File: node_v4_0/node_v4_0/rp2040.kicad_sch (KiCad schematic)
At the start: 29 parts, among them U1 RP2040, U2 W25Q128JVS, U7 PTS526 SK15 SMTR2 LFS, U8 PTS526 SK15 SMTR2 LFS

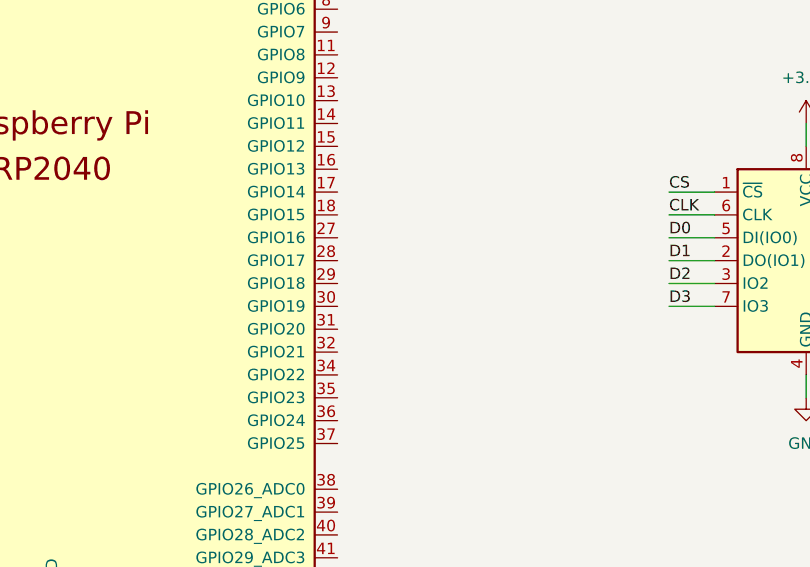
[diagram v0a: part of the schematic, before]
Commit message: more tracing, added RFM, added SIM, built power systems. converted to star ground
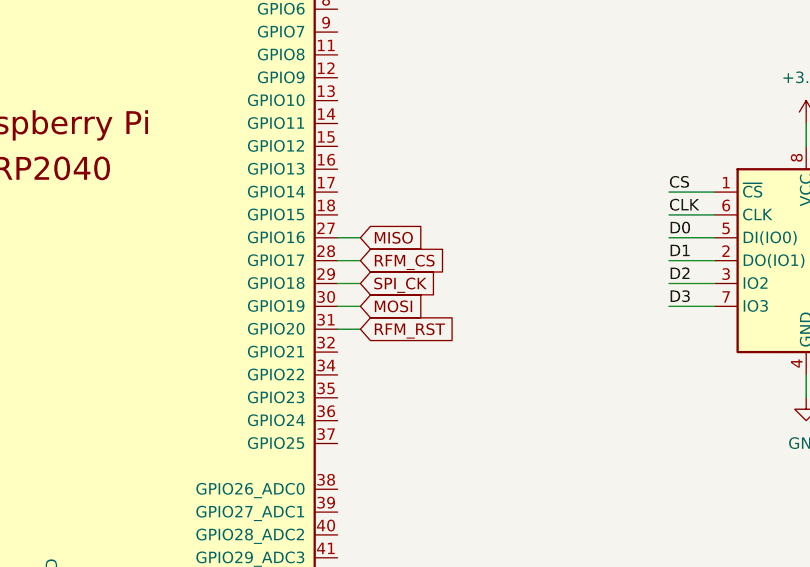
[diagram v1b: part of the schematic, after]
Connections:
- net MISO: now reaches U1.27 (GPIO16)
- net RFM_CS: now reaches U1.28 (GPIO17)
- net SPI_CK: now reaches U1.29 (GPIO18)
- net MOSI: now reaches U1.30 (GPIO19)
- net RFM_RST: now reaches U1.31 (GPIO20)
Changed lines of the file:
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@@
+	(wire
+		(pts
+			(xy 116.84 146.05) (xy 119.38 146.05)
+		)
+		(stroke
+			(width 0)
+			(type default)
+		)
+	)
 	(wire
 		(pts
@@
 	(wire
 		(pts
+			(xy 116.84 148.59) (xy 119.38 148.59)
+		)
+		(stroke
+			(width 0)
+			(type default)
+		)
+	)
+	(wire
+		(pts
 			(xy 46.99 153.67) (xy 53.34 153.67)
 		)
@@
 	(wire
 		(pts
+			(xy 116.84 143.51) (xy 119.38 143.51)
+		)
+		(stroke
+			(width 0)
+			(type default)
+		)
+	)
+	(wire
+		(pts
 			(xy 64.77 76.2) (xy 64.77 82.55)
 		)
@@
 	(wire
 		(pts
+			(xy 116.84 140.97) (xy 119.38 140.97)
+		)
+		(stroke
+			(width 0)
+			(type default)
+		)
+	)
+	(wire
+		(pts
 			(xy 38.1 43.18) (xy 38.1 44.45)
 		)
@@
 		(pts
 			(xy 86.36 76.2) (xy 86.36 82.55)
+		)
+		(stroke
+			(width 0)
+			(type default)
+		)
+	)
+	(wire
+		(pts
+			(xy 116.84 151.13) (xy 119.38 151.13)
 		)
 		(stroke
@@
 		)
 	)
+	(global_label "SPI_CK"
+		(shape input)
+		(at 119.38 146.05 0)
+		(fields_autoplaced yes)
+		(effects
+			(font
+				(size 1.27 1.27)
+			)
+			(justify left)
+		)
+		(property "Intersheetrefs" "${INTERSHEET_REFS}"
+			(at 128.9571 146.05 0)
+			(effects
+				(font
+					(size 1.27 1.27)
+				)
+				(justify left)
+				(hide yes)
+			)
+		)
+	)
+	(global_label "RFM_RST"
+		(shape input)
+		(at 119.38 151.13 0)
+		(fields_autoplaced yes)
+		(effects
+			(font
+				(size 1.27 1.27)
+			)
+			(justify left)
+		)
+		(property "Intersheetrefs" "${INTERSHEET_REFS}"
+			(at 130.5899 151.13 0)
+			(effects
+				(font
+					(size 1.27 1.27)
+				)
+				(justify left)
+				(hide yes)
+			)
+		)
+	)
+	(global_label "MISO"
+		(shape input)
+		(at 119.38 140.97 0)
+		(fields_autoplaced yes)
+		(effects
+			(font
+				(size 1.27 1.27)
+			)
+			(justify left)
+		)
+		(property "Intersheetrefs" "${INTERSHEET_REFS}"
+			(at 126.9614 140.97 0)
+			(effects
+				(font
+					(size 1.27 1.27)
+				)
+				(justify left)
+				(hide yes)
+			)
+		)
+	)
+	(global_label "RFM_CS"
+		(shape input)
+		(at 119.38 143.51 0)
+		(fields_autoplaced yes)
+		(effects
+			(font
+				(size 1.27 1.27)
+			)
+			(justify left)
+		)
+		(property "Intersheetrefs" "${INTERSHEET_REFS}"
+			(at 129.6223 143.51 0)
+			(effects
+				(font
+					(size 1.27 1.27)
+				)
+				(justify left)
+				(hide yes)
+			)
+		)
+	)
+	(global_label "MOSI"
+		(shape input)
+		(at 119.38 148.59 0)
+		(fields_autoplaced yes)
+		(effects
+			(font
+				(size 1.27 1.27)
+			)
+			(justify left)
+		)
+		(property "Intersheetrefs" "${INTERSHEET_REFS}"
+			(at 126.9614 148.59 0)
+			(effects
+				(font
+					(size 1.27 1.27)
+				)
+				(justify left)
+				(hide yes)
+			)
+		)
+	)
